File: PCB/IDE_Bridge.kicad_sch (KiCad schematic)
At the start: 93 parts, among them J1 IDE Connector, P1 USB_C_Plug_USB2.0, SW1 BOOTSEL, U1 74HCT245, U2 74HCT125, U3 74HCT125, U4 74HCT245, U5 RP2354B, U6 TVS, U7 LDO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

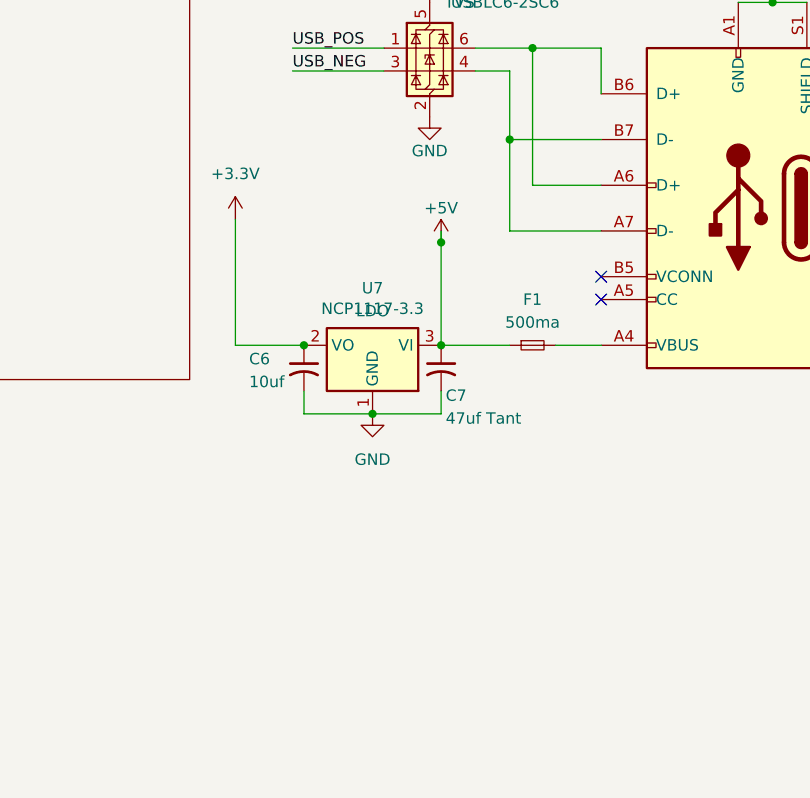
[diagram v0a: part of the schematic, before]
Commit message: Updated PCB
Rev .6 of PCB:  FIxed USB-C connector position, and added 5.1k pulldowns for CC1/CC2
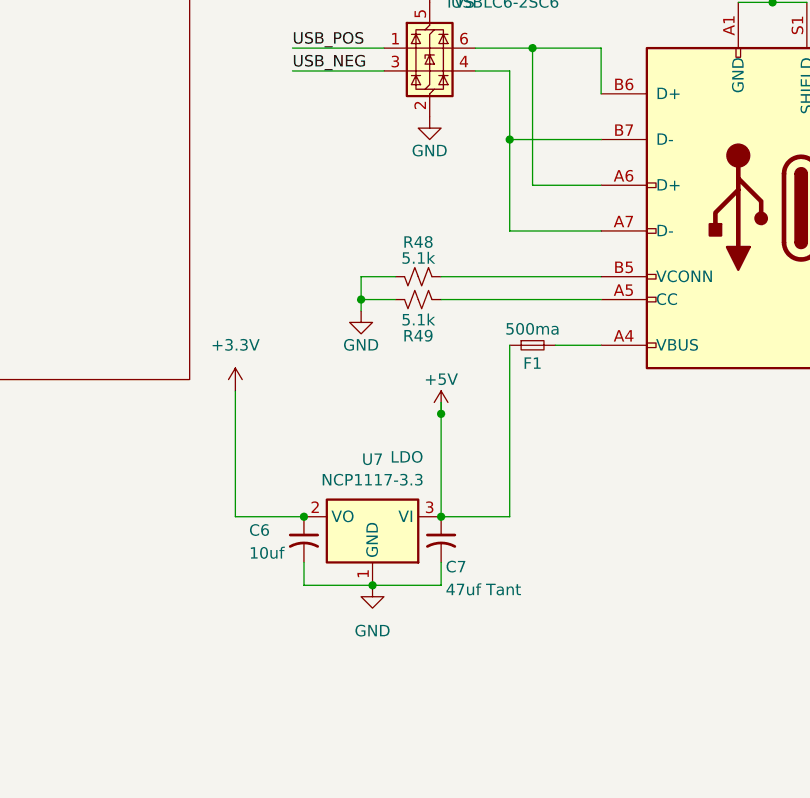
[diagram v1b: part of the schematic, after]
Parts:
- added R48, R49: 5.1k, Resistor_SMD:R_0402_1005Metric, symbol Device:R_Small_US
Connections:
- net GND: now also R48.1, R49.1
- net at P1.A5 (CC): now also R49.2
- net at P1.B5 (VCONN): now also R48.2
- no-connect marks 29 -> 27
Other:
- moved on the sheet: C6, C7, U7
